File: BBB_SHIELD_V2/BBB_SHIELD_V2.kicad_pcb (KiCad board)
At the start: 4 copper layers, 89.3 x 102.1 mm, 108 parts, among them J1 Screw_Terminal_01x04, J2 Conn_01x06_Male, J3 Conn_01x06_Male, J4 P8, J5 P9, J6 Screw_Terminal_01x02, J7 Conn_02x05_Odd_Even, Q1 Q_NMOS_GDS, SW1 SW_Push, SW2 SW_Push, U1 PTN78000WAH, U2 TC4432, U3 MCP1501_SOT-23-6, U4 CD74HCx4066, U5 CD74HCx4066, U6 TLV333, U7 MAX3232, U8 MAX3232

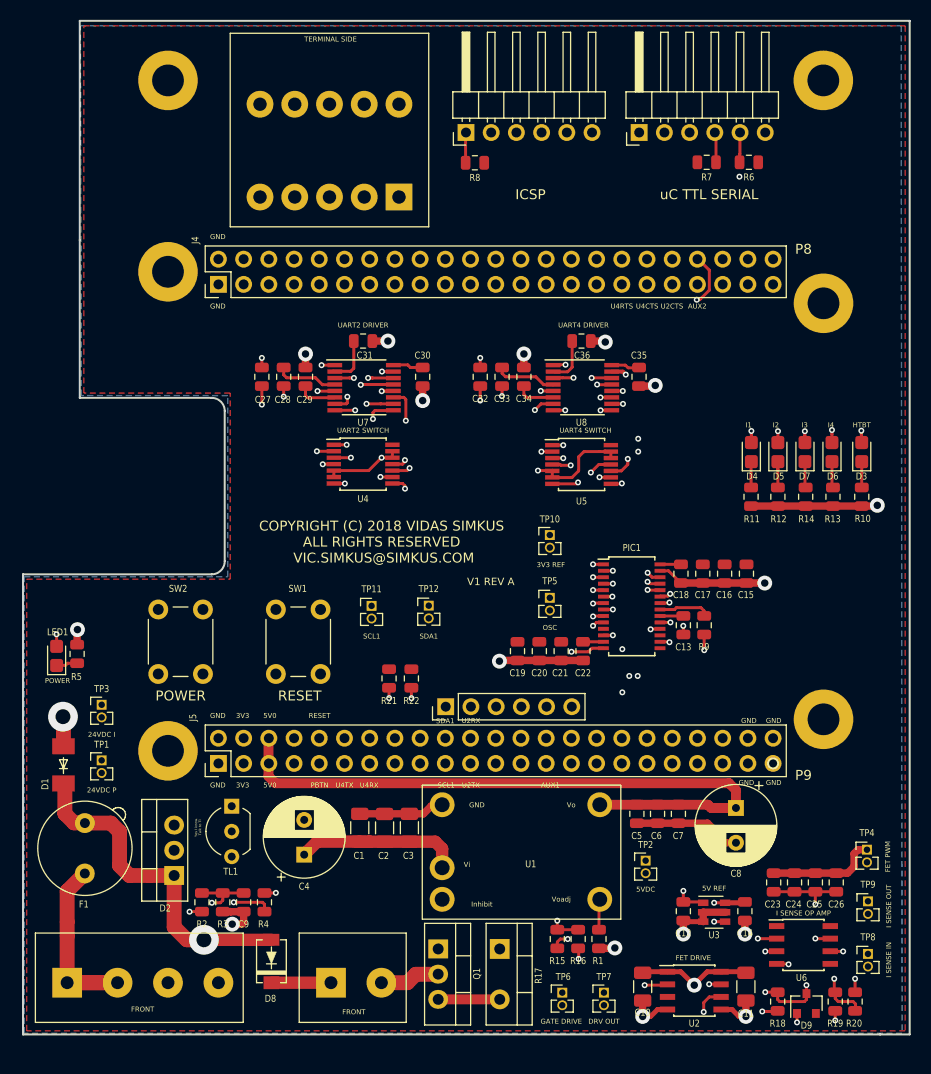
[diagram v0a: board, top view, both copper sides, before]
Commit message: Changed to high-side switching of power supply to boards.  Changed footprints to SOIC.  Misc other changes.
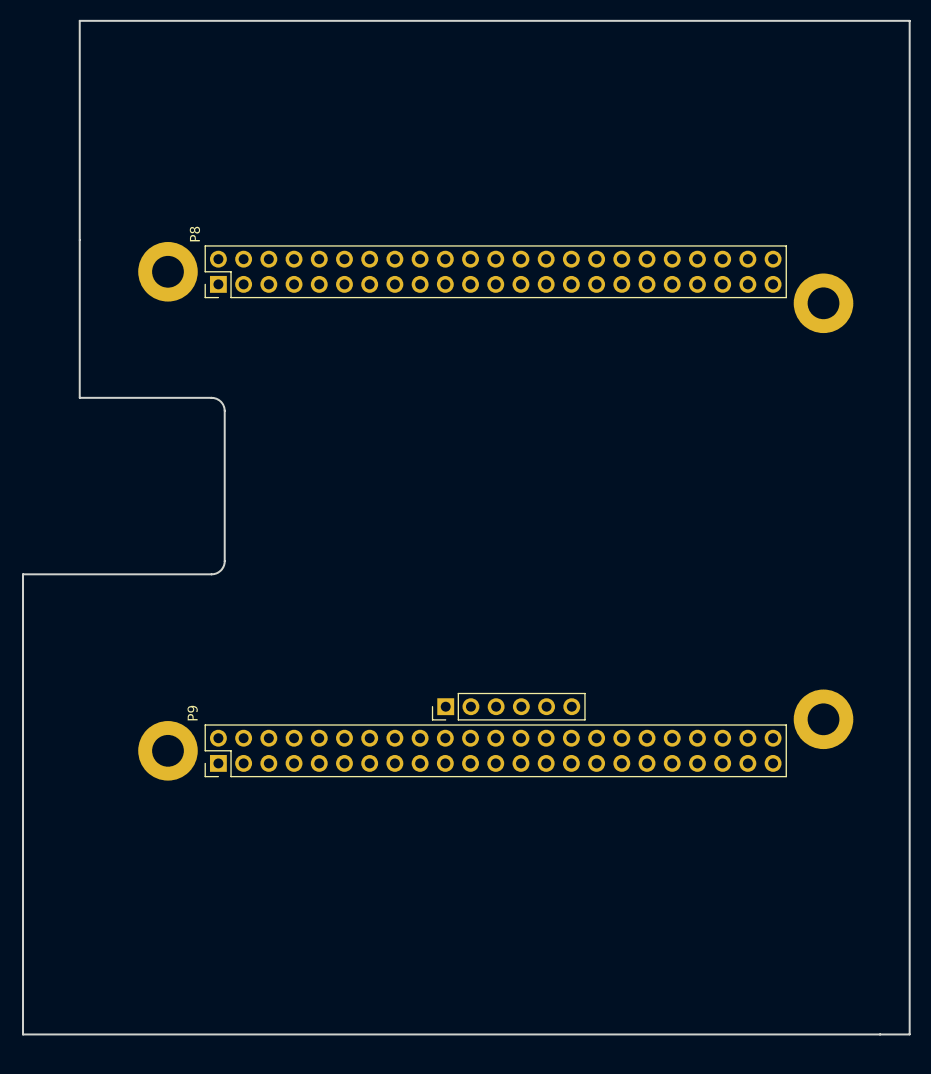
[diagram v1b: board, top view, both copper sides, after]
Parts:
- removed C1: 2.2uF 50V, Capacitor_SMD:C_1206_3216Metric
- removed C10, C11: 10uF, Capacitor_SMD:C_1206_3216Metric
- removed C12, C14, C17, C21, C25, C5: 1uF, Capacitor_SMD:C_0805_2012Metric
- removed C13: 10uF 10V, Capacitor_SMD:C_0805_2012Metric
- removed C15, C19, C23: 0.01uF, Capacitor_SMD:C_0805_2012Metric
- removed C16, C20, C24: .1uF, Capacitor_SMD:C_0805_2012Metric
- removed C18, C22, C26, C7: 10uF, Capacitor_SMD:C_0805_2012Metric
- removed C2: 1uF 50V, Capacitor_SMD:C_1206_3216Metric
- removed C27, C28, C29, C30, C31, C32, C33, C34, C35, C36: 0.1uF, Capacitor_SMD:C_0805_2012Metric
- removed C3: 10uF 50V, Capacitor_SMD:C_1206_3216Metric
- removed C4, C8: 180uF, Capacitor_THT:CP_Radial_D8.0mm_P3.50mm
- removed C6: 2.2uF, Capacitor_SMD:C_0805_2012Metric
- removed C9: 1nF, Capacitor_SMD:C_0805_2012Metric
- removed D1: D_ALT, CUSTOM_FOOTPRINTS:DO-214AA
- removed D2: 24V_TRIAC, Package_TO_SOT_THT:TO-220-3_Vertical
- removed D3, D4, D5, D6, D7: LED, LED_SMD:LED_0805_2012Metric_Castellated
- removed D8: D_ALT, CUSTOM_FOOTPRINTS:DO-221AC
- removed D9: BAS70-04, Package_TO_SOT_SMD:SOT-23
- removed F1: 24V_IN, Fuse:Fuseholder_TR5_Littelfuse_No560_No460
- removed J1: Screw_Terminal_01x04, CUSTOM_FOOTPRINTS:OSTTA044163
- removed J2, J3: Conn_01x06_Male, Connector_PinHeader_2.54mm:PinHeader_1x06_P2.54mm_Horizontal
- removed J6: Screw_Terminal_01x02, CUSTOM_FOOTPRINTS:OSTTA024163
- removed J7: Conn_02x05_Odd_Even, CUSTOM_FOOTPRINTS:PCB TERMINAL BLOCK - 1841526
- removed LED1: Vf=2V, LED_SMD:LED_0805_2012Metric_Castellated
- removed PIC1: PIC24FVXXKA302, Package_SO:TSSOP-28_4.4x9.7mm_P0.65mm
- removed Q1: Q_NMOS_GDS, Package_TO_SOT_THT:TO-220-3_Vertical
- removed R1: 21K 1%, Resistor_SMD:R_0805_2012Metric
- removed R10, R11, R12, R13, R14: 200 1%, Resistor_SMD:R_0805_2012Metric
- removed R15, R16, R18: 100R 1%, Resistor_SMD:R_0805_2012Metric
- removed R17: 0R2, Package_TO_SOT_THT:TO-220-2_Vertical
- removed R19: 1K5 1%, Resistor_SMD:R_0805_2012Metric
- removed R2: 23.2K 1%, Resistor_SMD:R_0805_2012Metric
- removed R20: 4K7 1%, Resistor_SMD:R_0805_2012Metric
- removed R21, R22: 5K, Resistor_SMD:R_0805_2012Metric
- removed R3: 2.49K 1%, Resistor_SMD:R_0805_2012Metric
- removed R4: 910 1%, Resistor_SMD:R_0805_2012Metric
- removed R5: 4.7K 1%, Resistor_SMD:R_0805_2012Metric
- removed R6, R7: 10K 5%, Resistor_SMD:R_0805_2012Metric
- removed R8: 10K, Resistor_SMD:R_0805_2012Metric
- removed R9: 150 1%, Resistor_SMD:R_0805_2012Metric
- removed the REF** at (185.0, 48.0)
- removed the REF** at (119.0, 48.0)
- removed SW1, SW2: SW_Push, Button_Switch_THT:SW_PUSH_6mm
- removed TL1: 24V_REF, CUSTOM_FOOTPRINTS:TO-92_Inline_Wide_TI
- removed TP1, TP10, TP11, TP12, TP2, TP4, TP5, TP6, TP7, TP8, TP9: TestPoint_2Pole, Connector_PinHeader_1.27mm:PinHeader_1x02_P1.27mm_Vertical
- removed TP3: TestPoint, Connector_PinHeader_1.27mm:PinHeader_1x02_P1.27mm_Vertical
- removed U1: PTN78000WAH, CUSTOM_FOOTPRINTS:PTN78000H
- removed U2: TC4432, Package_SO:SOIC-8_3.9x4.9mm_P1.27mm
- removed U3: MCP1501_SOT-23-6, Package_TO_SOT_SMD:SOT-23-6
- removed U4, U5: CD74HCx4066, Package_SO:TSSOP-14_4.4x5mm_P0.65mm
- removed U6: TLV333, Package_SO:SOIC-8_3.9x4.9mm_P1.27mm
- removed U7, U8: MAX3232, Package_SO:TSSOP-16_4.4x5mm_P0.65mm
- renumbered J4 to P8, J5 to P9
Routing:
- net _VDD_24V_PROT: track 191.9 -> 0.00 mm, vias 5 -> 0
- net GND: track 111.4 -> 0.00 mm, vias 26 -> 0
- net _VDD_5V_PROT: track 94.1 -> 0.00 mm, vias 2 -> 0
- net /CONTROLLER/~MCLR: track 91.5 -> 0.00 mm, vias 1 -> 0
- net /CONTROLLER/U1TX: track 86.5 -> 0.00 mm, vias 2 -> 0
- net /CONTROLLER/PGEC: track 77.9 -> 0.00 mm, vias 1 -> 0
- net /CONTROLLER/PWM_FET: track 77.0 -> 0.00 mm, vias 2 -> 0
- net /POWER_PROTECTION/VDD_24V: track 76.2 -> 0.00 mm
- net /CONTROLLER/I_SENSE: track 75.6 -> 0.00 mm, vias 3 -> 0
- net /CONTROLLER/PGED: track 72.5 -> 0.00 mm, vias 1 -> 0
- net /CONTROLLER/U1RX: track 67.2 -> 0.00 mm, vias 1 -> 0
- net /RS232/U2TXD: track 65.3 -> 0.00 mm, vias 1 -> 0
- net /CONTROLLER/3V3_REF: track 64.0 -> 0.00 mm, vias 2 -> 0
- net /BB_HEADERS/RS232_enable: track 62.9 -> 0.00 mm, vias 3 -> 0
- net /RS232/U2RXD: track 60.2 -> 0.00 mm, vias 1 -> 0
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- removed copper zone on B.Cu, net GND
- removed copper zone on F.Cu, net _VDD_3V3
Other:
- board text removed: "24VDC I"
- board text removed: "24VDC P"
- board text removed: "3V3"
- board text removed: "3V3 REF"
- board text removed: "5V REF"
- board text removed: "5V0"
- board text removed: "5VDC"
- board text removed: "AUX1"
- board text removed: "AUX2"
- board text removed: "COPYRIGHT (C) 2018 VIDAS SIMKUS ALL RIGHTS RESERVED VIC.SIMKUS@SIMKUS.COM"
- board text removed: "DRV OUT"
- board text removed: "FET DRIVE"
- board text removed: "FET PWM"
- board text removed: "GATE DRIVE"
- board text removed: "GND"
- board text removed: "HTBT"
- board text removed: "I SENSE IN"
- board text removed: "I SENSE OP AMP"
- board text removed: "I SENSE OUT"
- board text removed: "I1"
- board text removed: "I2"
- board text removed: "I3"
- board text removed: "I4"
- board text removed: "ICSP"
- board text removed: "NOTE: GROUND SWITCHED"
- board text removed: "OSC"
- board text removed: "P8"
- board text removed: "P9"
- board text removed: "PBTN"
- board text removed: "PGEC"
- board text removed: "PGED"
- board text removed: "POWER"
- board text removed: "RESET"
- board text removed: "RX"
- board text removed: "SCL1"
- board text removed: "SDA1"
- board text removed: "SYSTEM POWER SUPPLY"
- board text removed: "TX"
- board text removed: "U2CTS"
- board text removed: "U2CTSN"
- board text removed: "U2RTSN"
- board text removed: "U2RX"
- board text removed: "U2RXD"
- board text removed: "U2TX"
- board text removed: "U2TXD"
- board text removed: "U4CTS"
- board text removed: "U4CTSN"
- board text removed: "U4RTS"
- board text removed: "U4RTSN"
- board text removed: "U4RX"
- board text removed: "U4RXD"
- board text removed: "U4TX"
- board text removed: "U4TXD"
- board text removed: "UART2 DRIVER"
- board text removed: "UART2 SWITCH"
- board text removed: "UART4 DRIVER"
- board text removed: "UART4 SWITCH"
- board text removed: "V+"
- board text removed: "V-"
- board text removed: "V1 REV A"
- board text removed: "Yes I know. Talk to TI"
- board text removed: "uC TTL SERIAL"
- board text removed: "~MCLR"

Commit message: Schematic cleanup and refinement.
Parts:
- added C1: 1nF, Capacitor_SMD:C_0805_2012Metric, F.Cu at (152.4, 130.7)
- added C10: 10uF, Capacitor_SMD:C_0805_2012Metric, F.Cu at (173.4, 85.5)
- added C11: 0.01uF, Capacitor_SMD:C_0805_2012Metric, F.Cu at (155.9, 92.7)
- added C12: 0.1uF, Capacitor_SMD:C_0805_2012Metric, F.Cu at (155.9, 95.4)
- added C13: 1uF, Capacitor_SMD:C_0805_2012Metric, F.Cu at (155.9, 98.1)
- added C14: 10uF, Capacitor_SMD:C_0805_2012Metric, F.Cu at (155.9, 100.8)
- added C15: 0.01uF, Capacitor_SMD:C_0805_2012Metric, F.Cu at (141.6, 133.4)
- added C16: 0.1uF, Capacitor_SMD:C_0805_2012Metric, F.Cu at (141.6, 136.4)
- added C17: 1uF, Capacitor_SMD:C_0805_2012Metric, F.Cu at (141.6, 139.3)
- added C18: 10uF, Capacitor_SMD:C_0805_2012Metric, F.Cu at (141.6, 142.2)
- added C19: 0.01uF, Capacitor_SMD:C_0805_2012Metric, F.Cu at (152.5, 133.5)
- added C2: 0.1uF, Capacitor_SMD:C_0805_2012Metric, F.Cu at (135.8, 128.9)
- added C20: 0.1uF, Capacitor_SMD:C_0805_2012Metric, F.Cu at (152.5, 136.4)
- added C21: 1uF, Capacitor_SMD:C_0805_2012Metric, F.Cu at (152.5, 139.3)
- added C22: 10uF, Capacitor_SMD:C_0805_2012Metric, F.Cu at (152.5, 142.3)
- added C23: 0.1uF, Capacitor_SMD:C_0805_2012Metric, F.Cu at (137.7, 49.8)
- added C24: 0.1uF, Capacitor_SMD:C_0805_2012Metric, F.Cu at (169.1, 49.8)
- added C25: 0.1uF, Capacitor_SMD:C_0805_2012Metric, F.Cu at (124.0, 49.9)
- added C26: 0.1uF, Capacitor_SMD:C_0805_2012Metric, F.Cu at (124.0, 55.4)
- added C27: 0.1uF, Capacitor_SMD:C_0805_2012Metric, F.Cu at (155.1, 49.8)
- added C28: 0.1uF, Capacitor_SMD:C_0805_2012Metric, F.Cu at (155.0, 55.2)
- added C29: 0.1uF, Capacitor_SMD:C_0805_2012Metric, F.Cu at (124.0, 52.6)
- added C3: 10uF, Capacitor_SMD:C_1206_3216Metric, F.Cu at (141.4, 125.5)
- added C30: 0.1uF, Capacitor_SMD:C_0805_2012Metric, F.Cu at (155.0, 52.5)
- added C31: 0.1uF, Capacitor_SMD:C_0805_2012Metric, F.Cu at (124.0, 58.1)
- added C32: 0.1uF, Capacitor_SMD:C_0805_2012Metric, F.Cu at (155.0, 57.9)
- added C33: 10uF, Capacitor_SMD:C_1206_3216Metric, F.Cu at (178.1, 132.7)
- added C34: 10uF, Capacitor_SMD:C_1206_3216Metric, F.Cu at (178.1, 135.8)
- added C35: 10uF, Capacitor_SMD:C_1206_3216Metric, F.Cu at (162.3, 133.8)
- added C36: 10uF, Capacitor_SMD:C_1206_3216Metric, F.Cu at (162.3, 136.2)
- added C37: 2.2uF, Capacitor_SMD:C_1206_3216Metric, F.Cu at (162.3, 138.6)
- added C38: 2.2uF, Capacitor_SMD:C_1206_3216Metric, F.Cu at (162.3, 141.0)
- added C39: 10uF, Capacitor_SMD:C_1206_3216Metric, F.Cu at (178.0, 120.1)
- added C4: 1uF, Capacitor_SMD:C_0805_2012Metric, F.Cu at (131.8, 99.5)
- added C40: 10uF, Capacitor_SMD:C_1206_3216Metric, F.Cu at (178.0, 123.3)
- added C41: 10uF, Capacitor_SMD:C_1206_3216Metric, F.Cu at (162.3, 124.2)
- added C42: 10uF, Capacitor_SMD:C_1206_3216Metric, F.Cu at (162.3, 126.6)
- added C43: 2.2uF, Capacitor_SMD:C_1206_3216Metric, F.Cu at (162.3, 129.0)
- added C44: 2.2uF, Capacitor_SMD:C_1206_3216Metric, F.Cu at (162.3, 131.4)
- added C45: C, Capacitor_SMD:C_0805_2012Metric, F.Cu at (152.8, 78.4)
- added C5: 1uF, Capacitor_SMD:C_0805_2012Metric, F.Cu at (131.8, 107.5)
- added C6: 10uF, Capacitor_SMD:C_0805_2012Metric, F.Cu at (173.4, 88.2)
- added C7: 0.01uF, Capacitor_SMD:C_0805_2012Metric, F.Cu at (173.4, 77.4)
- added C8: 0.1uF, Capacitor_SMD:C_0805_2012Metric, F.Cu at (173.4, 80.1)
- added C9: 1uF, Capacitor_SMD:C_0805_2012Metric, F.Cu at (173.4, 82.8)
- added CONN5V5: Screw_Terminal_01x02, CUSTOM_FOOTPRINTS:OSTTA024163, F.Cu at (112.5, 101.9)
- added D1: 24V_TRIAC, Package_TO_SOT_THT:TO-220-3_Vertical, F.Cu at (120.9, 106.7)
- added D10: D_ALT, CUSTOM_FOOTPRINTS:COMCHIP_TO_277, F.Cu at (127.6, 124.6)
- added D11: D_ALT, CUSTOM_FOOTPRINTS:COMCHIP_TO_277, F.Cu at (129.8, 130.0)
- added D2: D_ALT, CUSTOM_FOOTPRINTS:DO-214AA, F.Cu at (120.9, 109.8)
- added D3: D_ALT, Diode_SMD:D_SOD-123F, F.Cu at (140.2, 128.9)
- added D4: LEDHMI1, LED_SMD:LED_0805_2012Metric_Castellated, F.Cu at (172.9, 97.5)
- added D5: LEDHMI2, LED_SMD:LED_0805_2012Metric_Castellated, F.Cu at (172.9, 100.9)
- added D6: LEDHMI3, LED_SMD:LED_0805_2012Metric_Castellated, F.Cu at (172.9, 104.2)
- added D7: LEDHMI4, LED_SMD:LED_0805_2012Metric_Castellated, F.Cu at (172.9, 107.6)
- added D8: LEDHTBT, LED_SMD:LED_0805_2012Metric_Castellated, F.Cu at (172.9, 110.9)
- added D9: D_ALT, CUSTOM_FOOTPRINTS:COMCHIP_TO_277, F.Cu at (129.8, 135.2)
- added DRVA1: MAX3232, Package_SO:SOIC-16_3.9x9.9mm_P1.27mm, F.Cu at (131.1, 54.1)
- added DRVB1: MAX3232, Package_SO:SOIC-16_3.9x9.9mm_P1.27mm, F.Cu at (162.4, 54.1)
- added F1: 24V_IN, Fuse:Fuseholder_TR5_Littelfuse_No560_No460, F.Cu at (107.2, 116.1)
- added J1: Screw_Terminal_01x04, CUSTOM_FOOTPRINTS:OSTTA044163, F.Cu at (112.5, 131.3)
- added J2: Conn_01x06_Male, CUSTOM_FOOTPRINTS:PinHeader_1x06_P2.54mm_Horizontal, F.Cu at (190.2, 94.6)
- added J3: Conn_01x06_Male, CUSTOM_FOOTPRINTS:PinHeader_1x06_P2.54mm_Horizontal, F.Cu at (190.2, 75.4)
- added J4: Conn_01x10_Female, CUSTOM_FOOTPRINTS:10_POS_SPRING_TERM, F.Cu at (137.7, 73.7)
- added LED1: LED, LED_SMD:LED_0805_2012Metric_Castellated, F.Cu at (121.9, 99.5)
- added P12V1: VX78XX, CUSTOM_FOOTPRINTS:Vx78-1000, F.Cu at (168.6, 122.3)
- added P5V1: VX78XX, CUSTOM_FOOTPRINTS:Vx78-1000, F.Cu at (168.6, 134.9)
- added PIC1: PIC24FVXXKA302, Package_SO:SOIC-28W_7.5x17.9mm_P1.27mm, F.Cu at (164.6, 85.7)
- added Q1: Q_NMOS_GDS, Package_TO_SOT_THT:TO-220-3_Vertical, F.Cu at (119.8, 122.2)
- added R1: 1K0, Resistor_SMD:R_0805_2012Metric, F.Cu at (156.1, 107.3)
- added R10: 10K, Resistor_SMD:R_0805_2012Metric, F.Cu at (181.5, 85.7)
- added R11: 200R, Resistor_SMD:R_0805_2012Metric, F.Cu at (177.0, 97.5)
- added R12: 200R, Resistor_SMD:R_0805_2012Metric, F.Cu at (177.0, 100.9)
- added R13: 10K, Resistor_SMD:R_0805_2012Metric, F.Cu at (181.5, 83.0)
- added R14: 200R, Resistor_SMD:R_0805_2012Metric, F.Cu at (177.0, 104.2)
- added R15: 200R, Resistor_SMD:R_0805_2012Metric, F.Cu at (177.0, 107.6)
- added R16: 200R, Resistor_SMD:R_0805_2012Metric, F.Cu at (176.9, 110.9)
- added R17: 200R, Resistor_SMD:R_0805_2012Metric, F.Cu at (160.2, 107.3)
- added R18: 5K6, Resistor_SMD:R_0805_2012Metric, F.Cu at (141.3, 111.0)
- added R19: 5K6, Resistor_SMD:R_0805_2012Metric, F.Cu at (141.2, 107.5)
- added R2: 1K0, Resistor_SMD:R_0805_2012Metric, F.Cu at (171.4, 72.3)
- added R20: 100R, Resistor_SMD:R_0805_2012Metric, F.Cu at (135.3, 123.6)
- added R21: 100R, Resistor_SMD:R_0805_2012Metric, F.Cu at (135.3, 120.8)
- added R23: 100R, Resistor_SMD:R_0805_2012Metric, F.Cu at (147.5, 139.4)
- added R24: 24K9, Resistor_SMD:R_0805_2012Metric, F.Cu at (147.5, 142.3)
- added R3: 1K0, Resistor_SMD:R_0805_2012Metric, F.Cu at (175.1, 72.4)
- added R4: 1K0, Resistor_SMD:R_0805_2012Metric, F.Cu at (160.2, 98.2)
- added R5: 910R, Resistor_SMD:R_0805_2012Metric, F.Cu at (147.8, 127.8)
- added R6: 23K2, Resistor_SMD:R_0805_2012Metric, F.Cu at (147.8, 130.7)
- added R7: 4K7, Resistor_SMD:R_0805_2012Metric, F.Cu at (126.2, 99.5)
- added R8: 2K49, Resistor_SMD:R_0805_2012Metric, F.Cu at (152.4, 127.8)
- added R9: 10K, Resistor_SMD:R_0805_2012Metric, F.Cu at (177.0, 94.7)
- added RS232SW_A1: CD74HCx4066, Package_SO:SOIC-14_3.9x8.7mm_P1.27mm, F.Cu at (146.7, 53.5)
- added RS232SW_B1: CD74HCx4066, Package_SO:SOIC-14_3.9x8.7mm_P1.27mm, F.Cu at (178.0, 53.5)
- added RSHUNT1: 0.010, CUSTOM_FOOTPRINTS:1206_WIDE_SHUNT, F.Cu at (125.4, 141.5)
- added TL1: 24V_REF, CUSTOM_FOOTPRINTS:TO-92_Inline_Wide_TI, F.Cu at (152.3, 123.1)
- added TP1: TestPoint, TestPoint:TestPoint_THTPad_D1.0mm_Drill0.5mm, F.Cu at (185.0, 118.6)
- added TP12V1: TestPoint, TestPoint:TestPoint_THTPad_D1.0mm_Drill0.5mm, F.Cu at (177.2, 127.4)
- added TP2: TEST_POINT, TestPoint:TestPoint_THTPad_D1.0mm_Drill0.5mm, F.Cu at (105.6, 109.8)
- added TP3V3REF1: TestPoint, TestPoint:TestPoint_THTPad_D1.0mm_Drill0.5mm, F.Cu at (135.8, 102.5)
- added TP5V1: TestPoint, TestPoint:TestPoint_THTPad_D1.0mm_Drill0.5mm, F.Cu at (177.2, 140.0)
- added TP7: TEST_POINT, Connector_PinHeader_1.27mm:PinHeader_1x02_P1.27mm_Vertical, F.Cu at (126.2, 120.9)
- added TPCLK1: TestPoint, TestPoint:TestPoint_THTPad_D1.0mm_Drill0.5mm, F.Cu at (156.8, 88.8)
- added TPFETOUT1: TestPoint, TestPoint:TestPoint_THTPad_D1.0mm_Drill0.5mm, F.Cu at (122.2, 132.7)
- added TPSCL1: TestPoint, Connector_PinHeader_1.27mm:PinHeader_1x01_P1.27mm_Vertical, F.Cu at (137.3, 111.0)
- added TPSDA1: TestPoint, Connector_PinHeader_1.27mm:PinHeader_1x01_P1.27mm_Vertical, F.Cu at (137.3, 107.5)
- added TPSHUNT1: TestPoint_2Pole, Connector_PinHeader_1.27mm:PinHeader_1x02_P1.27mm_Vertical, F.Cu at (136.8, 140.7)
- added U1: LTC7004, CUSTOM_FOOTPRINTS:MSOP-10, F.Cu at (137.9, 120.6)
- added U4: INA138, Package_TO_SOT_SMD:SOT-23-5, F.Cu at (136.8, 135.0)
- added U5: OPA340NA, Package_TO_SOT_SMD:SOT-23-5, F.Cu at (147.5, 135.6)
- added VREF3V1: MCP1501_SOT-23-6, Package_TO_SOT_SMD:SOT-23-6, F.Cu at (131.8, 103.7)
- added swP1: SW_Push, Button_Switch_THT:SW_PUSH_6mm, F.Cu at (144.8, 95.6)
- added swR1: SW_Push, Button_Switch_THT:SW_PUSH_6mm, F.Cu at (144.8, 82.2)
- P8: value P8 -> BBCONN
- P9: value P9 -> BBCONN
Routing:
- net _VDD_24V_PROT: track 0.00 -> 192.1 mm, vias 0 -> 6
- net _VDD_5V_PROT: track 0.00 -> 128.6 mm, vias 0 -> 2
- net GND: track 0.00 -> 119.6 mm, vias 0 -> 69
- net /BB_HEADERS/RS232_enable: track 0.00 -> 104.1 mm, vias 0 -> 12
- net /BB_HEADERS/uart2_txd_sw: track 0.00 -> 94.1 mm, vias 0 -> 3
- net /BB_HEADERS/uart2_rxd_sw: track 0.00 -> 93.5 mm, vias 0 -> 3
- net /CONTROLLER/I_SENSE: track 0.00 -> 77.4 mm, vias 0 -> 3
- net /RS232/U2RXD: track 0.00 -> 75.1 mm, vias 0 -> 2
- net /BB_HEADERS/uart4_rxd_sw: track 0.00 -> 75.1 mm, vias 0 -> 2
- net /BB_HEADERS/SDA1: track 0.00 -> 71.2 mm, vias 0 -> 4
- net /BB_HEADERS/SCL1: track 0.00 -> 70.5 mm, vias 0 -> 3
- net /BB_HEADERS/uart4_txd_sw: track 0.00 -> 68.9 mm, vias 0 -> 3
- net /RS232/U2TXD: track 0.00 -> 68.5 mm, vias 0 -> 2
- net /CONTROLLER/3V3_REF: track 0.00 -> 64.7 mm, vias 0 -> 4
- net _VDD_3V3: track 0.00 -> 61.4 mm
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- added copper zone on B.Cu, net GND
- added copper zone on F.Cu, net _VDD_24V_PROT
- added copper zone on F.Cu, net _VDD_3V3
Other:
- net class 24V_PROT removed
- net class 5V_PROT removed
- net class Default: trace_width 0.3 -> 0.2; via_dia 0.6 -> 0.5
- net class POWER added: clearance 0.2, trace_width 0.4, via_dia 0.8, via_drill 0.4
- board text added: "1"
- board text added: "11"
- board text added: "12"
- board text added: "17"
- board text added: "18"
- board text added: "2"
- board text added: "23"
- board text added: "24"
- board text added: "24V IN"
- board text added: "24V OUT"
- board text added: "29"
- board text added: "30"
- board text added: "37"
- board text added: "38"
- board text added: "45"
- board text added: "46"
- board text added: "5"
- board text added: "5V UNFUSED P9 [5,6]"
- board text added: "6"
- board text added: "CTS"
- board text added: "Copyright (C) 2019 Vidas Simkus All Rights Reserved"
- board text added: "GND"
- board text added: "HTBT"
- board text added: "LED1"
- board text added: "LED2"
- board text added: "LED3"
- board text added: "LED4"
- board text added: "MCLR"
- board text added: "P8"
- board text added: "P9"
- board text added: "PGEC"
- board text added: "PGED"
- board text added: "POWER"
- board text added: "RESET"
- board text added: "RTS"
- board text added: "RX"
- board text added: "TP12V"
- board text added: "TP3V3REF"
- board text added: "TP5V"
- board text added: "TPCLK"
- board text added: "TPFETDRV"
- board text added: "TPGD"
- board text added: "TPGND"
- board text added: "TPISENSE"
- board text added: "TPSCL"
- board text added: "TPSDA"
- board text added: "TX"
- board text added: "U4"
- board text added: "VDD3V3"
- board text added: "Vidas Simkus https://www.simkus.com"

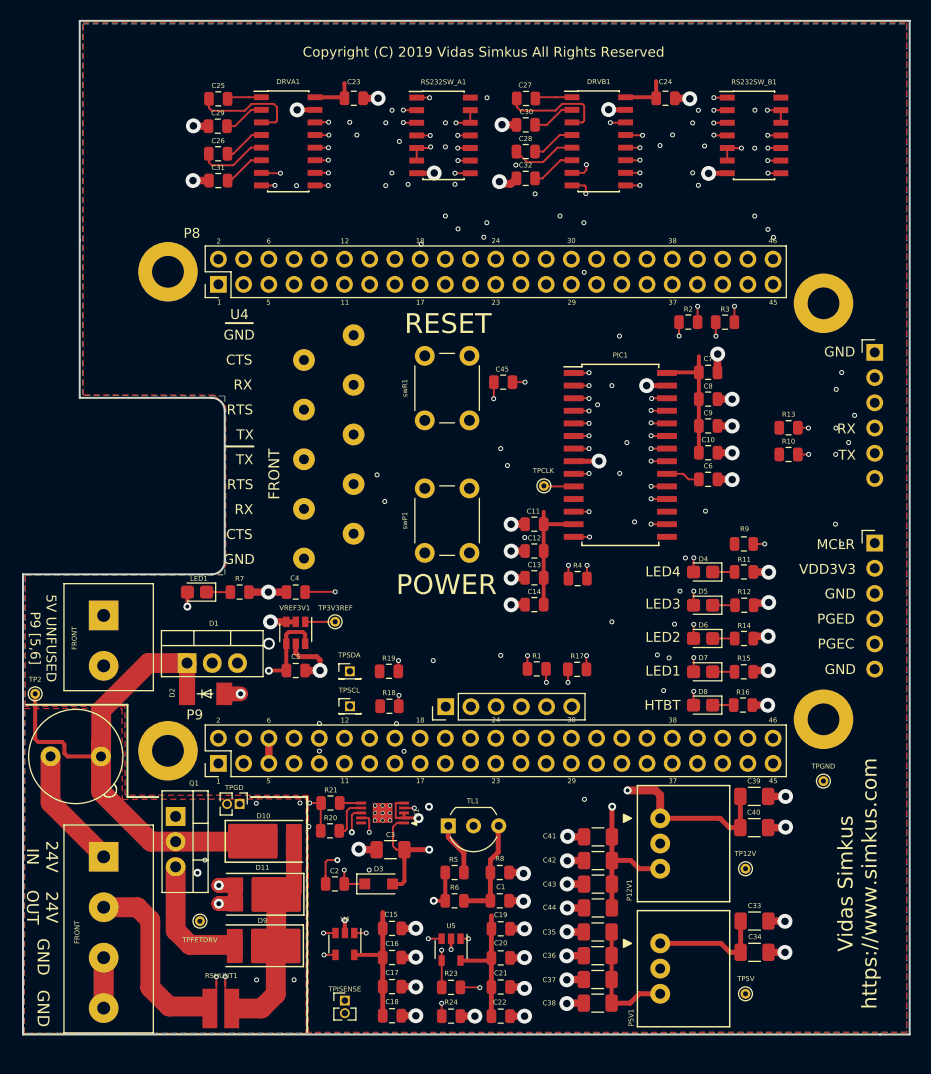
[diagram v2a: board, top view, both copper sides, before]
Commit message: Submited to board fab.
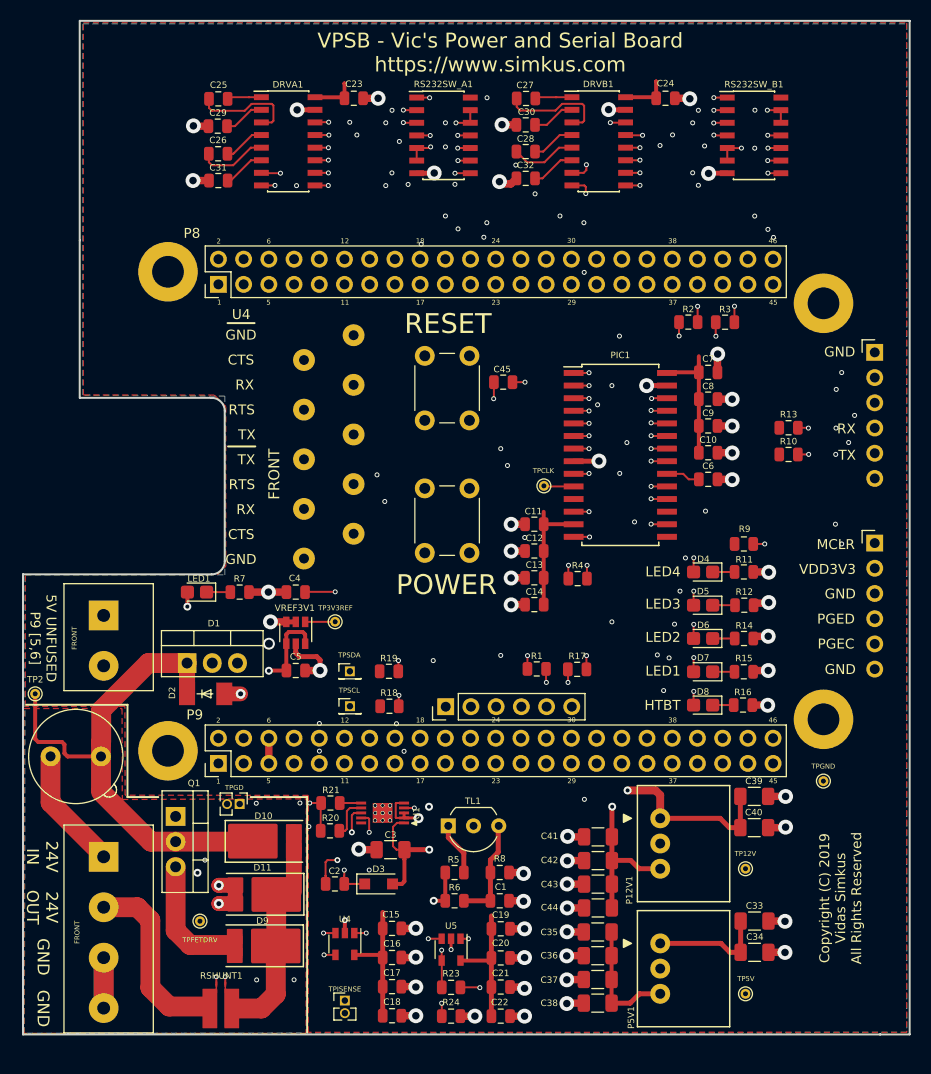
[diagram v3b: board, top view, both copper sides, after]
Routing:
- net Net-(C25-Pad1): track 11.3 -> 10.7 mm
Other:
- board text added: "VPSB - Vic's Power and Serial Board https://www.simkus.com"
- board text removed: "Vidas Simkus https://www.simkus.com"
